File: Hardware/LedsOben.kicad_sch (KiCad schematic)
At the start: 40 parts

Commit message: assign remaining LCSC numbers and change R_sense of LED drivers
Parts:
- added R16, R26, R27, R8: 3.3, Resistor_SMD:R_0805_2012Metric, symbol Device:R_Small
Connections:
- net GND: now also R16.2, R26.2, R27.2, R8.2
- new net LedTreiber1/R_{sense}: R8.1
- new net LedTreiber2/R_{sense}: R26.1
- new net LedTreiber3/R_{sense}: R27.1
- new net LedTreiber5/R_{sense}: R16.1
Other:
- sheet LedTreiber1 ports: added R_{sense}; removed none
- sheet LedTreiber2 ports: added R_{sense}; removed none
- sheet LedTreiber3 ports: added R_{sense}; removed none
- sheet LedTreiber5 ports: added R_{sense}; removed none

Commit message: remove LCSC numbers from silkscreen (bug in jlcpcb-tools)
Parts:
- D10, D11, D12, D13, D14, D15, D16, D17, D18, D19, D20, D21, D22, D23, D4, D9: LCSC (none) -> C784540
- D25, D27, D28, D29, D30, D31, D32, D33, D35, D36, D37, D38, D39, D40, D41, D42: LCSC (none) -> C264473
- R16, R26, R27, R8: LCSC (none) -> C16257
- R18, R19, R28, R29, R30, R31, R32, R4: LCSC (none) -> C17561

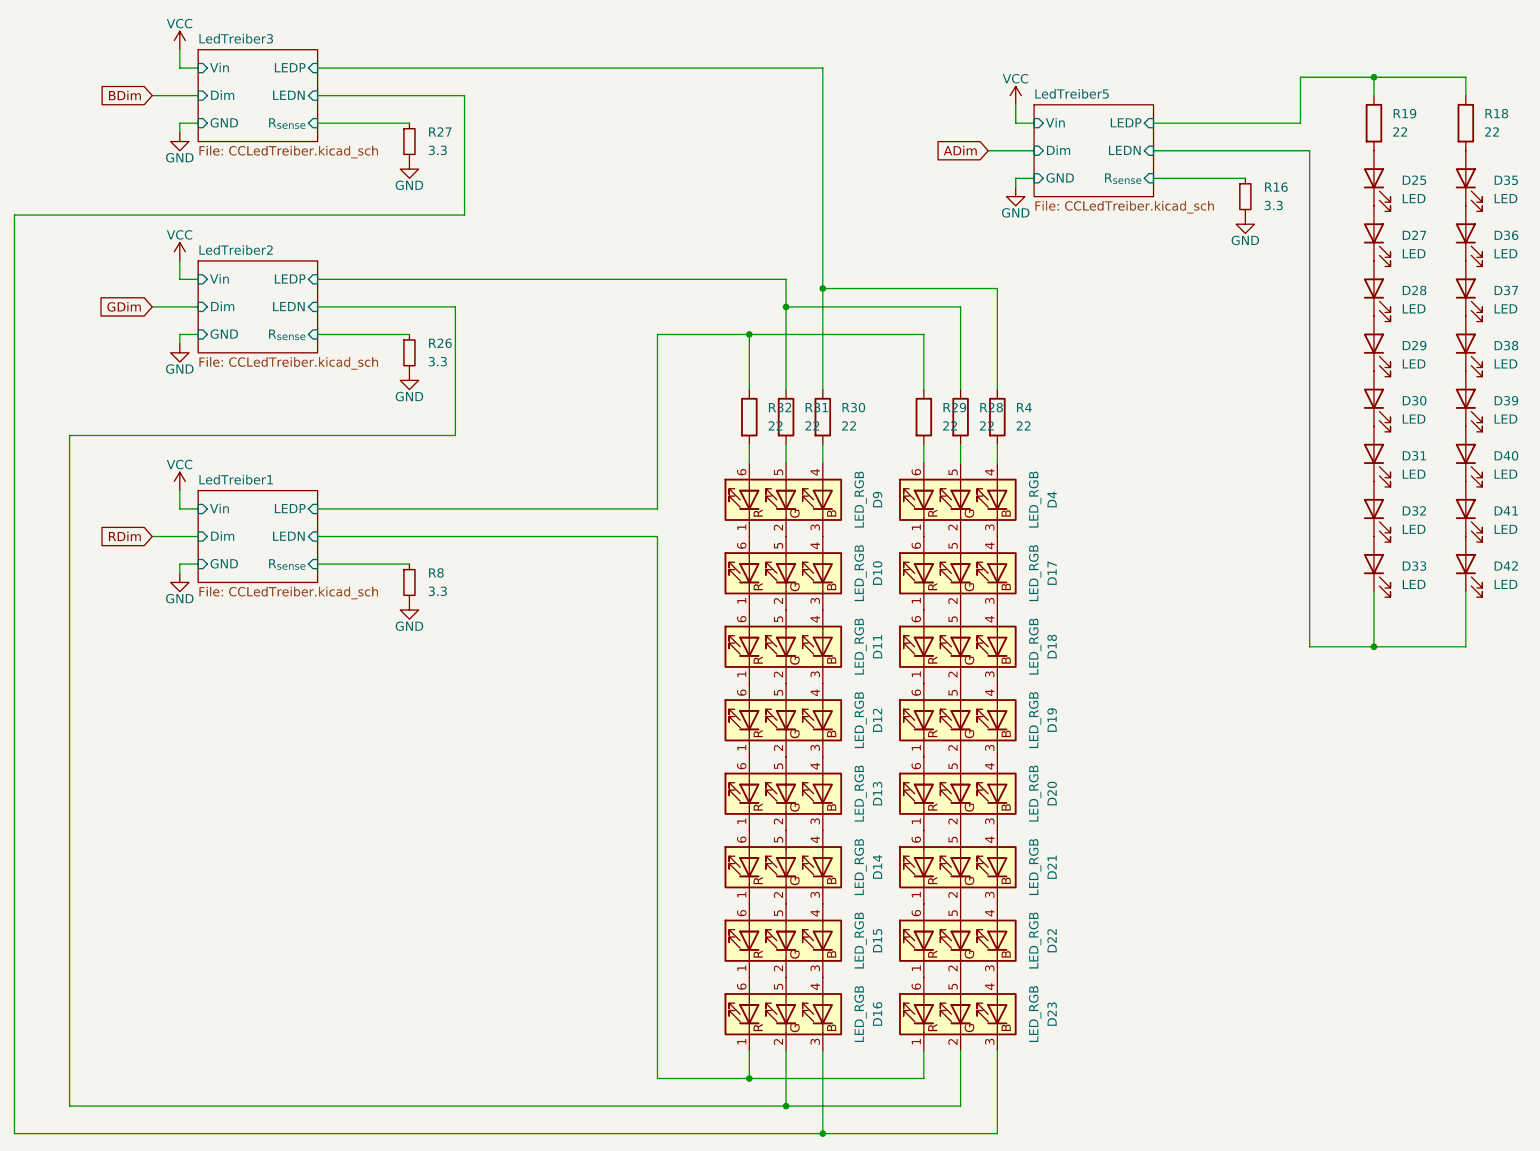
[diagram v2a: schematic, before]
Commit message: some fixes and BOM optimization, heatsinking, etc
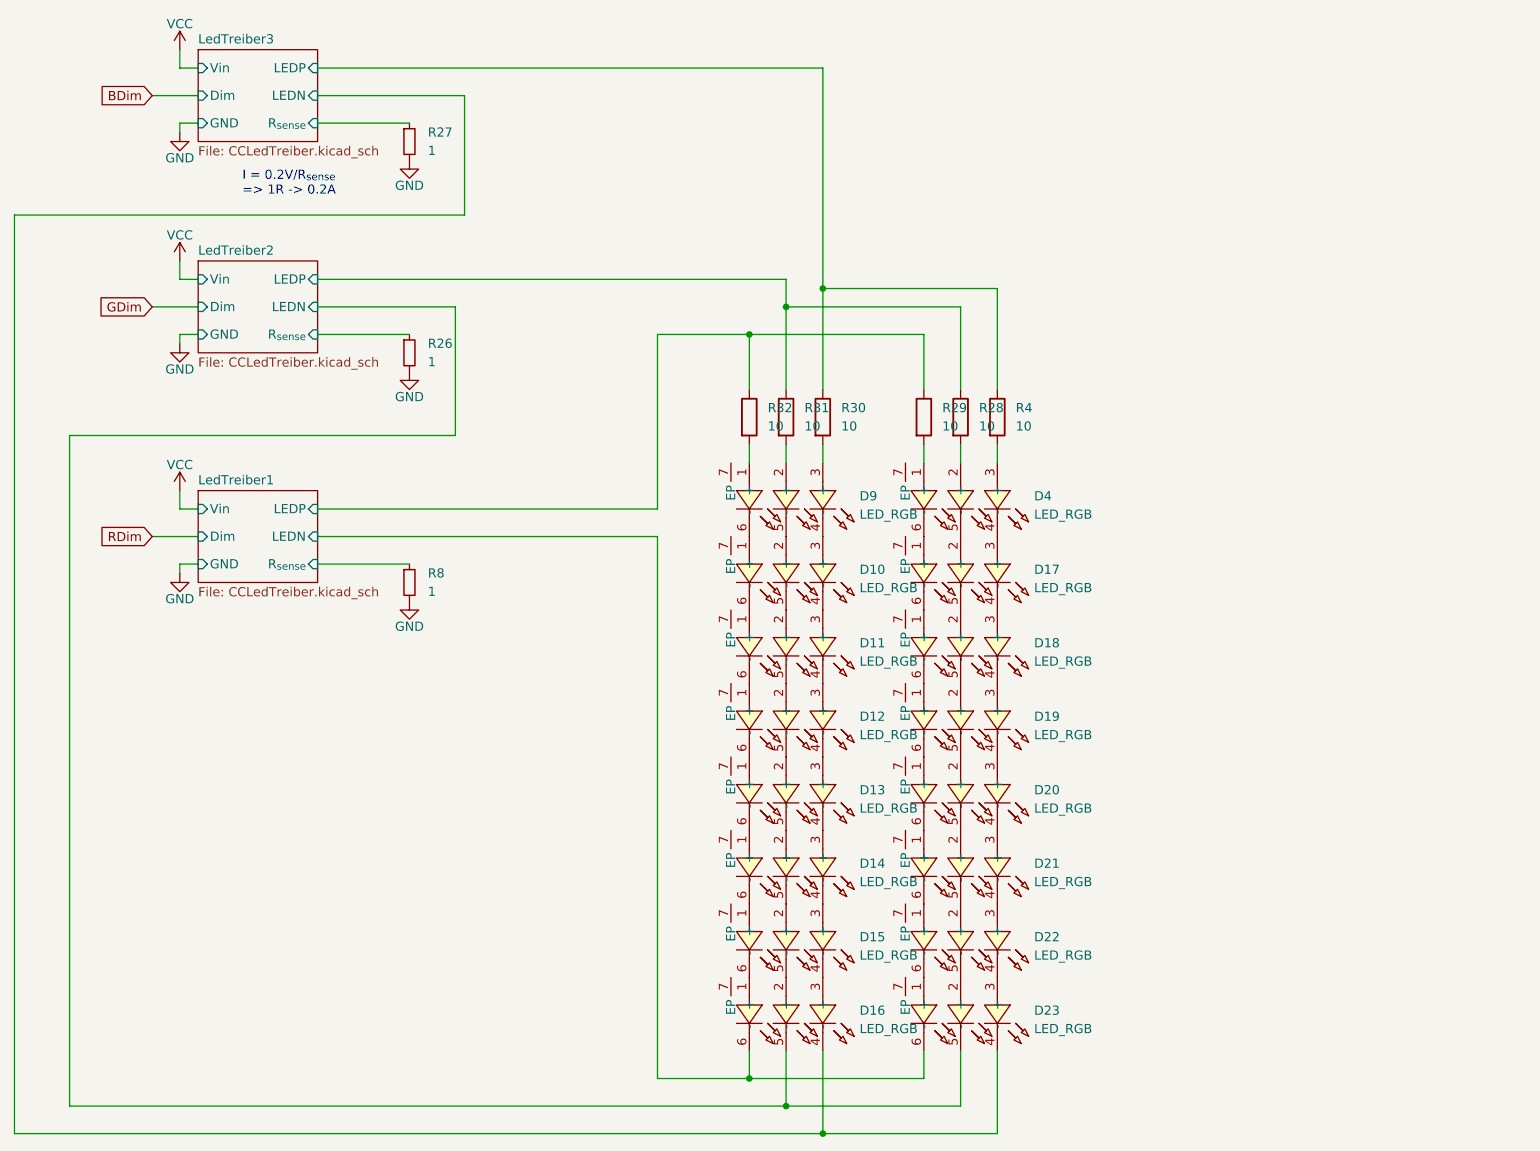
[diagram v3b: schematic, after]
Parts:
- removed D25, D27, D28, D29, D30, D31, D32, D33, D35, D36, D37, D38, D39, D40, D41, D42: LED, LED_SMD:LED_0603_1608Metric, symbol Device:LED
- removed R16: 3.3, Resistor_SMD:R_0805_2012Metric, symbol Device:R_Small
- removed R18, R19: 22, Resistor_SMD:R_0805_2012Metric, symbol Device:R
- D10, D11, D12, D13, D14, D15, D16, D17, D18, D19, D20, D21, D22, D23, D4, D9: footprint LCSC:LED-SMD_6P-L5.0-W5.0-TL_TC5050RGBF08 -> LCSC:LED-SMD_6P-L5.0-W5.0-BL_TC5053RGBE60; symbol Device:LED_RGB -> LCSC:TC5053RGBE60-3CJH-GF09
- R26, R27, R8: value 3.3 -> 1
- R28, R29, R30, R31, R32, R4: value 22 -> 10; LCSC C17561 -> C17415
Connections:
- net LedTreiber1/LEDN: now also D16.6 (-), D23.6 (-); no longer D16.1 (RK), D23.1 (RK)
- net LedTreiber2/LEDN: now also D16.5 (-), D23.5 (-); no longer D16.2 (GK), D23.2 (GK)
- net LedTreiber3/LEDN: now also D16.4 (-), D23.4 (-); no longer D16.3 (BK), D23.3 (BK)
- net at R29.2: now also D4.1 (+); no longer D4.6 (RA)
- net at D20.1 (+): now also D19.6 (-); no longer D21.6 (RA)
- net at D20.2 (+): now also D19.5 (-); no longer D21.5 (GA)
- net at D20.3 (+): now also D19.4 (-); no longer D21.4 (BA)
- net at D20.4 (-): now also D21.3 (+); no longer D19.3 (BK)
- net at D20.5 (-): now also D21.2 (+); no longer D19.2 (GK)
- net at D20.6 (-): now also D21.1 (+); no longer D19.1 (RK)
- net at R32.2: now also D9.1 (+); no longer D9.6 (RA)
- net at D13.1 (+): now also D12.6 (-); no longer D14.6 (RA)
- net at D13.2 (+): now also D12.5 (-); no longer D14.5 (GA)
- net at D13.3 (+): now also D12.4 (-); no longer D14.4 (BA)
- net at D13.4 (-): now also D14.3 (+); no longer D12.3 (BK)
- net at D13.5 (-): now also D14.2 (+); no longer D12.2 (GK)
- net at D13.6 (-): now also D14.1 (+); no longer D12.1 (RK)
- net at R4.2: now also D4.3 (+); no longer D4.4 (BA)
- net at R28.2: now also D4.2 (+); no longer D4.5 (GA)
- net at D15.1 (+): now also D14.6 (-); no longer D16.6 (RA)
- net at D15.2 (+): now also D14.5 (-); no longer D16.5 (GA)
- net at D15.3 (+): now also D14.4 (-); no longer D16.4 (BA)
- net at D15.4 (-): now also D16.3 (+); no longer D14.3 (BK)
- net at D15.5 (-): now also D16.2 (+); no longer D14.2 (GK)
- net at D15.6 (-): now also D16.1 (+); no longer D14.1 (RK)
- net at D11.1 (+): now also D10.6 (-); no longer D12.6 (RA)
- net at D11.2 (+): now also D10.5 (-); no longer D12.5 (GA)
- net at D11.3 (+): now also D10.4 (-); no longer D12.4 (BA)
- net at D11.4 (-): now also D12.3 (+); no longer D10.3 (BK)
- net at D11.5 (-): now also D12.2 (+); no longer D10.2 (GK)
- net at D11.6 (-): now also D12.1 (+); no longer D10.1 (RK)
- net at D22.3 (+): now also D21.4 (-); no longer D23.4 (BA)
- net at D22.2 (+): now also D21.5 (-); no longer D23.5 (GA)
- net at D22.1 (+): now also D21.6 (-); no longer D23.6 (RA)
- net at D9.2 (+): now also R31.2; no longer D10.5 (GA)
- net at D9.3 (+): now also R30.2; no longer D10.4 (BA)
- net at D9.4 (-): now also D10.3 (+); no longer R30.2
- net at D9.5 (-): now also D10.2 (+); no longer R31.2
- net at D22.4 (-): now also D23.3 (+); no longer D21.3 (BK)
- net at D22.5 (-): now also D23.2 (+); no longer D21.2 (GK)
- net at D22.6 (-): now also D23.1 (+); no longer D21.1 (RK)
- net at D18.1 (+): now also D17.6 (-); no longer D19.6 (RA)
- net at D18.2 (+): now also D17.5 (-); no longer D19.5 (GA)
- net at D18.3 (+): now also D17.4 (-); no longer D19.4 (BA)
- net at D18.4 (-): now also D19.3 (+); no longer D17.3 (BK)
- net at D18.5 (-): now also D19.2 (+); no longer D17.2 (GK)
- net at D18.6 (-): now also D19.1 (+); no longer D17.1 (RK)
- new net: D10.1 (+), D9.6 (-)
- new net: D17.3 (+), D4.4 (-)
- new net: D17.2 (+), D4.5 (-)
- new net: D17.1 (+), D4.6 (-)
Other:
- removed sheet LedTreiber5
- note added: "I = 0.2V/R_{sense} => 1R -> 0.2A"

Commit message: silkscreen and stuff
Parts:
- R26, R27, R8: LCSC C16257 -> C25271
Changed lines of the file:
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@@
 			)
 		)
-		(property "LCSC" "C16257"
+		(property "LCSC" "C25271"
 			(at 86.36 41.9099 0)
 			(effects
@@
 			)
 		)
-		(property "LCSC" "C16257"
+		(property "LCSC" "C25271"
 			(at 86.36 71.1199 0)
 			(effects
@@
 			)
 		)
-		(property "LCSC" "C16257"
+		(property "LCSC" "C25271"
 			(at 86.36 102.8699 0)
 			(effects

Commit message: final touches for v1.0
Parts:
- D10, D11, D12, D13, D14, D15, D16, D17, D18, D19, D20, D21, D22, D23, D4, D9: LCSC C784540 -> (none)
- R26, R27, R8: LCSC C25271 -> (none)
- R28, R29, R30, R31, R32, R4: LCSC C17415 -> (none)
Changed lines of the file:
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@@
-			)
-		)
-		(property "LCSC" "C17415"
-			(at 157.48 80.0099 0)
-			(effects
-				(font
-					(size 1.27 1.27)
-				)
-				(hide yes)
 			)
 		)
@@
 			)
 		)
-		(property "LCSC" "C25271"
-			(at 86.36 41.9099 0)
-			(effects
-				(font
-					(size 1.27 1.27)
-				)
-				(hide yes)
-			)
-		)
 		(pin "1"
 		)
@@
 			)
 		)
-		(property "LCSC" "C784540"
-			(at 147.32 133.35 0)
-			(effects
-				(font
-					(size 1.27 1.27)
-				)
-				(hide yes)
-			)
-		)
 		(pin "1"
 		)
@@
 			)
 		)
-		(property "LCSC" "C17415"
-			(at 133.35 80.0099 0)
-			(effects
-				(font
-					(size 1.27 1.27)
-				)
-				(hide yes)
-			)
-		)
 		(pin "2"
 		)
@@
 			)
 		)
-		(property "LCSC" "C784540"
-			(at 123.19 133.35 0)
-			(effects
-				(font
-					(size 1.27 1.27)
-				)
-				(hide yes)
-			)
-		)
 		(pin "1"
 		)
@@
 			)
 		)
-		(property "LCSC" "C17415"
-			(at 167.64 80.0099 0)
-			(effects
-				(font
-					(size 1.27 1.27)
-				)
-				(hide yes)
-			)
-		)
 		(pin "2"
 		)
@@
 			)
 		)
-		(property "LCSC" "C17415"
-			(at 162.56 80.0099 0)
-			(effects
-				(font
-					(size 1.27 1.27)
-				)
-				(hide yes)
-			)
-		)
 		(pin "2"
 		)
@@
 			)
 		)
-		(property "LCSC" "C784540"
-			(at 123.19 153.67 0)
-			(effects
-				(font
-					(size 1.27 1.27)
-				)
-				(hide yes)
-			)
-		)
 		(pin "1"
 		)
@@
 			)
 		)
-		(property "LCSC" "C784540"
-			(at 123.19 113.03 0)
-			(effects
-				(font
-					(size 1.27 1.27)
-				)
-				(hide yes)
-			)
-		)
 		(pin "1"
 		)
@@
 		(property "Description" "Resistor, small symbol"
 			(at 83.82 72.39 0)
-			(effects
-				(font
-					(size 1.27 1.27)
-				)
-				(hide yes)
-			)
-		)
-		(property "LCSC" "C25271"
-			(at 86.36 71.1199 0)
 			(effects
 				(font
@@
 			)
 		)
-		(property "LCSC" "C784540"
-			(at 147.32 163.83 0)
-			(effects
-				(font
-					(size 1.27 1.27)
-				)
-				(hide yes)
-			)
-		)
 		(pin "1"
 		)
@@
 			)
 		)
-		(property "LCSC" "C784540"
-			(at 123.19 92.71 0)
-			(effects
-				(font
-					(size 1.27 1.27)
-				)
-				(hide yes)
-			)
-		)
 		(pin "1"
 		)
@@
 			)
 		)
-		(property "LCSC" "C17415"
-			(at 138.43 80.0099 0)
-			(effects
-				(font
-					(size 1.27 1.27)
-				)
-				(hide yes)
-			)
-		)
 		(pin "2"
 		)
@@
 			)
 		)
-		(property "LCSC" "C784540"
-			(at 147.32 153.67 0)
-			(effects
-				(font
-					(size 1.27 1.27)
-				)
-				(hide yes)
-			)
-		)
 		(pin "1"
 		)
@@
 			)
 		)
-		(property "LCSC" "C784540"
-			(at 147.32 113.03 0)
-			(effects
-				(font
-					(size 1.27 1.27)
-				)
-				(hide yes)
-			)
-		)
 		(pin "1"
 		)
@@
 			)
 		)
-		(property "LCSC" "C784540"
-			(at 147.32 123.19 0)
-			(effects
-				(font
-					(size 1.27 1.27)
-				)
-				(hide yes)
-			)
-		)
 		(pin "1"
 		)
@@
 		(property "Description" ""
 			(at 160.02 143.51 0)
-			(effects
-				(font
-					(size 1.27 1.27)
-				)
-				(hide yes)
-			)
-		)
-		(property "LCSC" "C784540"
-			(at 147.32 143.51 0)
 			(effects
 				(font
@@
 			)
 		)
-		(property "LCSC" "C784540"
-			(at 147.32 92.71 0)
-			(effects
-				(font
-					(size 1.27 1.27)
-				)
-				(hide yes)
-			)
-		)
 		(pin "1"
 		)
@@
 			)
 		)
-		(property "LCSC" "C784540"
-			(at 123.19 143.51 0)
-			(effects
-				(font
-					(size 1.27 1.27)
-				)
-				(hide yes)
-			)
-		)
 		(pin "1"
 		)
@@
 			)
 		)
-		(property "LCSC" "C25271"
-			(at 86.36 102.8699 0)
-			(effects
-				(font
-					(size 1.27 1.27)
-				)
-				(hide yes)
-			)
-		)
 		(pin "1"
 		)
@@
 			)
 		)
-		(property "LCSC" "C784540"
-			(at 123.19 123.19 0)
-			(effects
-				(font
-					(size 1.27 1.27)
-				)
-				(hide yes)
-			)
-		)
 		(pin "1"
 		)
@@
 			)
 		)
-		(property "LCSC" "C784540"
-			(at 123.19 102.87 0)
-			(effects
-				(font
-					(size 1.27 1.27)
-				)
-				(hide yes)
-			)
-		)
 		(pin "1"
 		)
@@
 			)
 		)
-		(property "LCSC" "C784540"
-			(at 123.19 163.83 0)
-			(effects
-				(font
-					(size 1.27 1.27)
-				)
-				(hide yes)
-			)
-		)
 		(pin "1"
 		)
@@
 			)
 		)
-		(property "LCSC" "C17415"
-			(at 143.51 80.0099 0)
-			(effects
-				(font
-					(size 1.27 1.27)
-				)
-				(hide yes)
-			)
-		)
 		(pin "2"
 		)
@@
 			(effects
 				(font
-					(size 1.27 1.27)
-				)
-				(hide yes)
-			)
-		)
-		(property "LCSC" "C784540"
-			(at 147.32 102.87 0)
-			(effects
-				(font

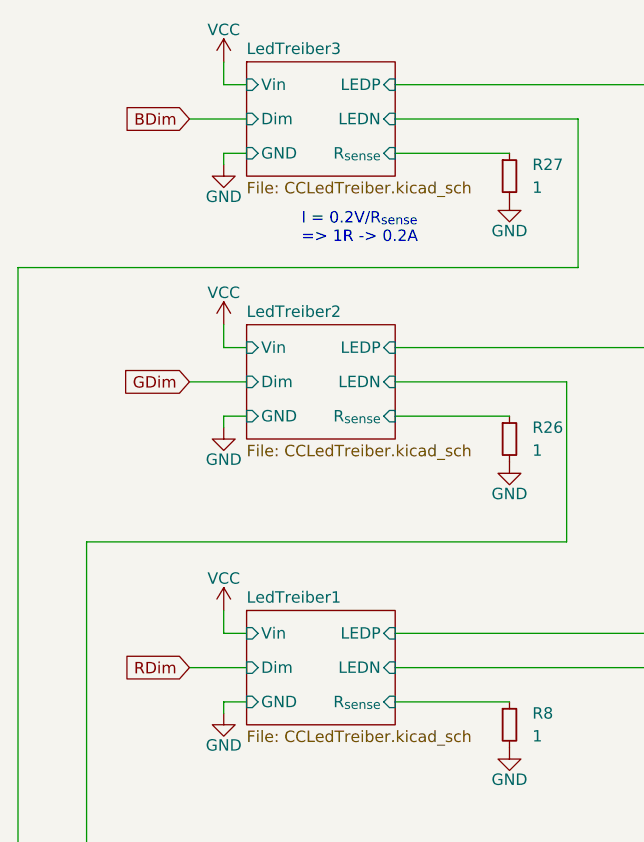
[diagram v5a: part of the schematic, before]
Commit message: update RGB mapping in KiCad
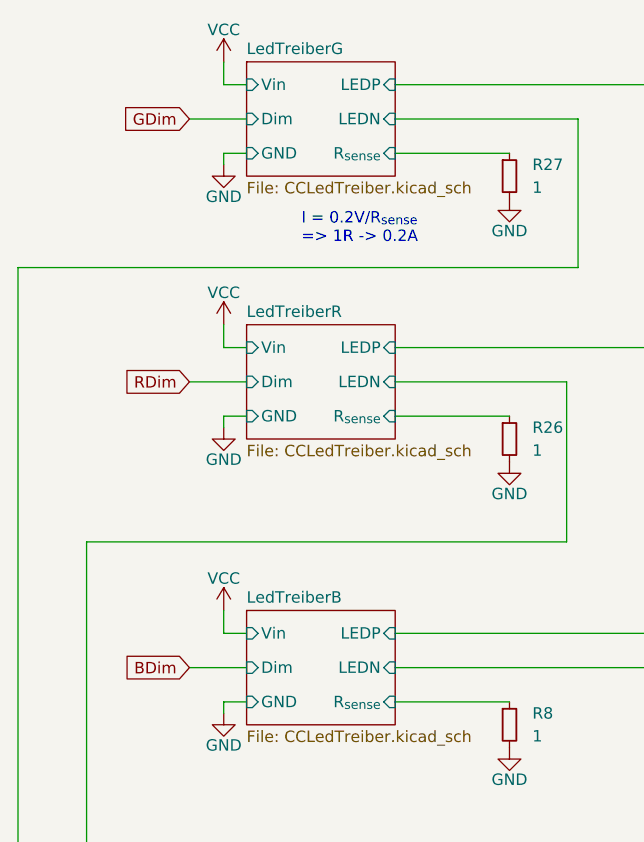
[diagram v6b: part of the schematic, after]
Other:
- sheet LedTreiber1 renamed LedTreiberB
- sheet LedTreiber2 renamed LedTreiberR
- sheet LedTreiber3 renamed LedTreiberG
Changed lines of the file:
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@@
 	(global_label "GDim"
 		(shape input)
-		(at 48.26 66.04 180)
+		(at 48.26 36.83 180)
 		(fields_autoplaced yes)
 		(effects
@@
 		)
 		(property "Intersheetrefs" "${INTERSHEET_REFS}"
-			(at 40.4367 66.04 0)
+			(at 40.4367 36.83 0)
 			(effects
 				(font
@@
 	(global_label "RDim"
 		(shape input)
-		(at 48.26 97.79 180)
+		(at 48.26 66.04 180)
 		(fields_autoplaced yes)
 		(effects
@@
 		)
 		(property "Intersheetrefs" "${INTERSHEET_REFS}"
-			(at 40.4367 97.79 0)
+			(at 40.4367 66.04 0)
 			(effects
 				(font
@@
 	(global_label "BDim"
 		(shape input)
-		(at 48.26 36.83 180)
+		(at 48.26 97.79 180)
 		(fields_autoplaced yes)
 		(effects
@@
 		)
 		(property "Intersheetrefs" "${INTERSHEET_REFS}"
-			(at 40.4367 36.83 0)
+			(at 40.4367 97.79 0)
 			(effects
 				(font
@@
 			(color 0 0 0 0.0000)
 		)
-		(property "Sheetname" "LedTreiber1"
+		(property "Sheetname" "LedTreiberB"
 			(at 54.61 90.7284 0)
 			(effects
@@
 			(color 0 0 0 0.0000)
 		)
-		(property "Sheetname" "LedTreiber2"
+		(property "Sheetname" "LedTreiberR"
 			(at 54.61 58.9784 0)
 			(effects
@@
 			(color 0 0 0 0.0000)
 		)
-		(property "Sheetname" "LedTreiber3"
+		(property "Sheetname" "LedTreiberG"
 			(at 54.61 29.7684 0)
 			(effects
